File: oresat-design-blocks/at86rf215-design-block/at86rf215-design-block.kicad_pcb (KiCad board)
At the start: 4 copper layers, 69.4 x 52.5 mm, 61 parts, among them J1 SMA, J2 USB4105-GF-A, J4 SMA, J7 SMA, J8 SMA, J9 Screw_Terminal_01x02, SW1 RESET, U1 AT86RF215, U2 LP2985AIM5-1.8_NOPB, U3 2450FB15A050E, U5 QPC1022, U7 NCS2-62+, X1 TXETALSANF-26.000000

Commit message: more routing progress
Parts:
- moved C27 15.6 mm to (125.4, 78.7), turned to 0 degrees
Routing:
- net Net-(J7-In): track 0.00 -> 3.11 mm
- net Net-(J4-In): track 0.00 -> 3.01 mm
- net Net-(J8-In): track 0.00 -> 2.99 mm
- net Net-(C19-Pad1): track 0.00 -> 2.93 mm
- net Net-(C19-Pad2): track 0.00 -> 2.72 mm
- net Net-(C20-Pad2): track 0.00 -> 2.54 mm
- net Net-(C17-Pad1): track 1.66 -> 3.32 mm
- net Net-(C18-Pad2): track 1.66 -> 3.31 mm
- net Net-(U5-RF_COM): track 0.00 -> 1.59 mm
- net Net-(C20-Pad1): track 0.00 -> 1.59 mm
- net GND: vias 55 -> 58
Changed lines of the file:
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@@
 	(footprint "oresat-passives:0402-C"
 		(layer "F.Cu")
-		(at 140.97 79.545 -90)
+		(at 125.38 78.67)
 		(descr "<b>0402 (metric 1005) tight 'IPC-C'</b>\n<br>In house package for minimum spacing based on IPC-7351B.")
 		(property "Reference" "C27"
-			(at -0.7 -0.6 90)
+			(at -0.7 -0.6 0)
 			(layer "F.SilkS")
 			(effects
@@
 					(thickness 0.125)
 				)
-				(justify right top)
+				(justify left bottom)
 			)
 		)
 		(property "Value" "100p"
-			(at -0.7 1.4 90)
+			(at -0.7 1.4 0)
 			(layer "F.Fab")
 			(effects
@@
 					(thickness 0.12)
 				)
-				(justify right top)
+				(justify left bottom)
 			)
 		)
 		(property "Datasheet" "~"
-			(at 0 0 90)
+			(at 0 0 0)
 			(layer "F.Fab")
 			(hide yes)
@@
 		)
 		(property "Description" "CAP CER 100PF 50V C0G/NP0 0402"
-			(at 0 0 90)
+			(at 0 0 0)
 			(layer "F.Fab")
 			(hide yes)
@@
 		)
 		(property "DPN" "490-GCM1555C1H101GA16DCT-ND "
-			(at 0 0 270)
+			(at 0 0 0)
 			(unlocked yes)
 			(layer "F.Fab")
@@
 		)
 		(property "MFR" "Murata Electronics"
-			(at 0 0 270)
+			(at 0 0 0)
 			(unlocked yes)
 			(layer "F.Fab")
@@
 		)
 		(property "MPN" "GCM1555C1H101GA16D "
-			(at 0 0 270)
+			(at 0 0 0)
 			(unlocked yes)
 			(layer "F.Fab")
@@
 		)
 		(property "DIS" "DigiKey"
-			(at 0 0 270)
+			(at 0 0 0)
 			(unlocked yes)
 			(layer "F.Fab")
@@
 		)
 		(fp_line
+			(start -0.795 -0.395)
+			(end -0.795 0.395)
+			(stroke
+				(width 0.01)
+				(type solid)
+			)
+			(layer "F.CrtYd")
+		)
+		(fp_line
 			(start -0.795 0.395)
 			(end 0.795 0.395)
@@
 		)
 		(fp_line
+			(start 0.795 -0.395)
+			(end -0.795 -0.395)
+			(stroke
+				(width 0.01)
+				(type solid)
+			)
+			(layer "F.CrtYd")
+		)
+		(fp_line
 			(start 0.795 0.395)
 			(end 0.795 -0.395)
@@
 		)
 		(fp_line
-			(start -0.795 -0.395)
-			(end -0.795 0.395)
-			(stroke
-				(width 0.01)
-				(type solid)
-			)
-			(layer "F.CrtYd")
-		)
-		(fp_line
-			(start 0.795 -0.395)
-			(end -0.795 -0.395)
-			(stroke
-				(width 0.01)
-				(type solid)
-			)
-			(layer "F.CrtYd")
+			(start -0.525 -0.275)
+			(end 0.525 -0.275)
+			(stroke
+				(width 0.05)
+				(type solid)
+			)
+			(layer "F.Fab")
 		)
 		(fp_line
@@
 		)
 		(fp_line
+			(start 0.525 -0.275)
+			(end 0.525 0.275)
+			(stroke
+				(width 0.05)
+				(type solid)
+			)
+			(layer "F.Fab")
+		)
+		(fp_line
 			(start 0.525 0.275)
 			(end -0.525 0.275)
-			(stroke
-				(width 0.05)
-				(type solid)
-			)
-			(layer "F.Fab")
-		)
-		(fp_line
-			(start -0.525 -0.275)
-			(end 0.525 -0.275)
-			(stroke
-				(width 0.05)
-				(type solid)
-			)
-			(layer "F.Fab")
-		)
-		(fp_line
-			(start 0.525 -0.275)
-			(end 0.525 0.275)
 			(stroke
 				(width 0.05)
@@
 		)
 		(pad "1" smd roundrect
-			(at -0.45 0 270)
+			(at -0.45 0)
 			(size 0.5 0.6)
 			(layers "F.Cu" "F.Mask" "F.Paste")
@@
 		)
 		(pad "2" smd roundrect
-			(at 0.45 0 270)
+			(at 0.45 0)
 			(size 0.5 0.6)
 			(layers "F.Cu" "F.Mask" "F.Paste")
@@
 		(start 125.3286 82.1686)
 		(end 125.33 82.17)
-		(width 0.2)
+		(width 0.25)
 		(layer "F.Cu")
 		(net 20)
@@
 		(start 122.7525 82.1686)
 		(end 125.3286 82.1686)
-		(width 0.2)
+		(width 0.25)
 		(layer "F.Cu")
 		(net 20)
@@
 	)
 	(via
+		(at 140.22 84.91)
+		(size 0.4572)
+		(drill 0.254)
+		(layers "F.Cu" "B.Cu")
+		(free yes)
+		(net 25)
+	)
+	(via
 		(at 130.85 79.685001)
 		(size 0.4572)
@@
 	)
 	(via
+		(at 137.1 86.37)
+		(size 0.4572)
+		(drill 0.254)
+		(layers "F.Cu" "B.Cu")
+		(free yes)
+		(net 25)
+	)
+	(via
 		(at 123.335 86.6386)
+		(size 0.4572)
+		(drill 0.254)
+		(layers "F.Cu" "B.Cu")
+		(free yes)
+		(net 25)
+	)
+	(via
+		(at 141.74 84.9)
 		(size 0.4572)
 		(drill 0.254)
@@
 	)
 	(segment
+		(start 128.54 82.17)
+		(end 129.44 82.17)
+		(width 0.25)
+		(layer "F.Cu")
+		(net 38)
+	)
+	(segment
 		(start 126.88 82.17)
 		(end 128.53 82.17)
@@
 	)
 	(segment
+		(start 128.535 82.175)
+		(end 128.54 82.17)
+		(width 0.25)
+		(layer "F.Cu")
+		(net 38)
+	)
+	(segment
+		(start 129.44 82.17)
+		(end 129.6114 82.3414)
+		(width 0.25)
+		(layer "F.Cu")
+		(net 38)
+	)
+	(segment
 		(start 128.53 82.23)
 		(end 128.535 82.235)
@@
 	)
 	(segment
+		(start 129.6114 82.3414)
+		(end 130.120001 82.3414)
+		(width 0.25)
+		(layer "F.Cu")
+		(net 38)
+	)
+	(segment
 		(start 128.535 83.75)
 		(end 126.88 83.75)
@@
 		(layer "F.Cu")
 		(net 39)
+	)
+	(segment
+		(start 128.535 83.75)
+		(end 129.48 83.75)
+		(width 0.25)
+		(layer "F.Cu")
+		(net 39)
+	)
+	(segment
+		(start 129.48 83.75)
+		(end 129.6386 83.5914)
+		(width 0.25)
+		(layer "F.Cu")
+		(net 39)
+	)
+	(segment
+		(start 129.6386 83.5914)
+		(end 130.120001 83.5914)
+		(width 0.25)
+		(layer "F.Cu")
+		(net 39)
+	)
+	(segment
+		(start 132.75 82.3414)
+		(end 134.135 82.3414)
+		(width 0.127)
+		(layer "F.Cu")
+		(net 40)
+	)
+	(segment
+		(start 131.419999 82.3414)
+		(end 132.75 82.3414)
+		(width 0.127)
+		(layer "F.Cu")
+		(net 40)
+	)
+	(segment
+		(start 137.1 82.3414)
+		(end 137.1 83.8564)
+		(width 0.127)
+		(layer "F.Cu")
+		(net 41)
+	)
+	(segment
+		(start 135.685 82.3414)
+		(end 137.1 82.3414)
+		(width 0.127)
+		(layer "F.Cu")
+		(net 41)
+	)
+	(segment
+		(start 138.75 82.3414)
+		(end 140.2186 82.3414)
+		(width 0.127)
+		(layer "F.Cu")
+		(net 42)
+	)
+	(segment
+		(start 140.2186 82.3414)
+		(end 140.22 82.34)
+		(width 0.127)
+		(layer "F.Cu")
+		(net 42)
+	)
+	(segment
+		(start 140.22 82.34)
+		(end 141.755 82.34)
+		(width 0.127)
+		(layer "F.Cu")
+		(net 42)
+	)
+	(segment
+		(start 141.755 82.34)
+		(end 141.76 82.345)
+		(width 0.127)
+		(layer "F.Cu")
+		(net 42)
 	)
 	(segment
@@
 		(net 50)
 	)
+	(segment
+		(start 132.155799 78.68)
+		(end 132.1608 78.685001)
+		(width 0.127)
+		(layer "F.Cu")
+		(net 53)
+	)
+	(segment
+		(start 129.619999 78.68)
+		(end 132.155799 78.68)
+		(width 0.127)
+		(layer "F.Cu")
+		(net 53)
+	)
+	(segment
+		(start 133.7108 78.685001)
+		(end 133.7108 77.1008)
+		(width 0.127)
+		(layer "F.Cu")
+		(net 54)
+	)
+	(segment
+		(start 133.7108 77.1008)
+		(end 133.71 77.1)
+		(width 0.127)
+		(layer "F.Cu")
+		(net 54)
+	)
+	(segment
+		(start 135.1892 78.683401)
+		(end 135.1908 78.685001)
+		(width 0.127)
+		(layer "F.Cu")
+		(net 55)
+	)
+	(segment
+		(start 135.1892 77.1)
+		(end 135.1892 78.683401)
+		(width 0.127)
+		(layer "F.Cu")
+		(net 55)
+	)
+	(segment
+		(start 149.07 79.99)
+		(end 152.1775 79.99)
+		(width 0.127)
+		(layer "F.Cu")
+		(net 57)
+	)
+	(segment
+		(start 149.18 71.62)
+		(end 152.16625 71.62)
+		(width 0.127)
+		(layer "F.Cu")
+		(net 58)
+	)
+	(segment
+		(start 152.16625 71.62)
+		(end 152.1675 71.62125)
+		(width 0.127)
+		(layer "F.Cu")
+		(net 58)
+	)
 	(zone

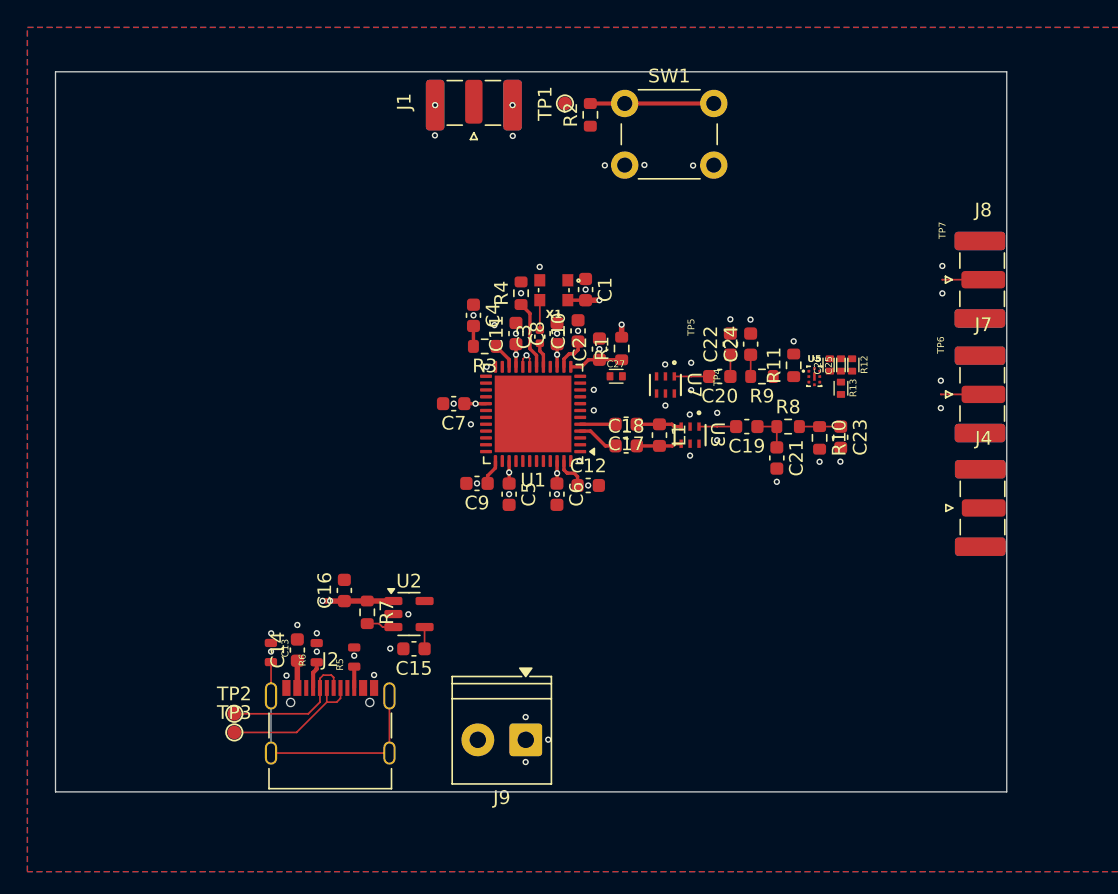
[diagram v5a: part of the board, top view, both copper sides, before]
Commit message: completed initial routing, changed pin out and added voltage divider to QPC1022 CTRL pin
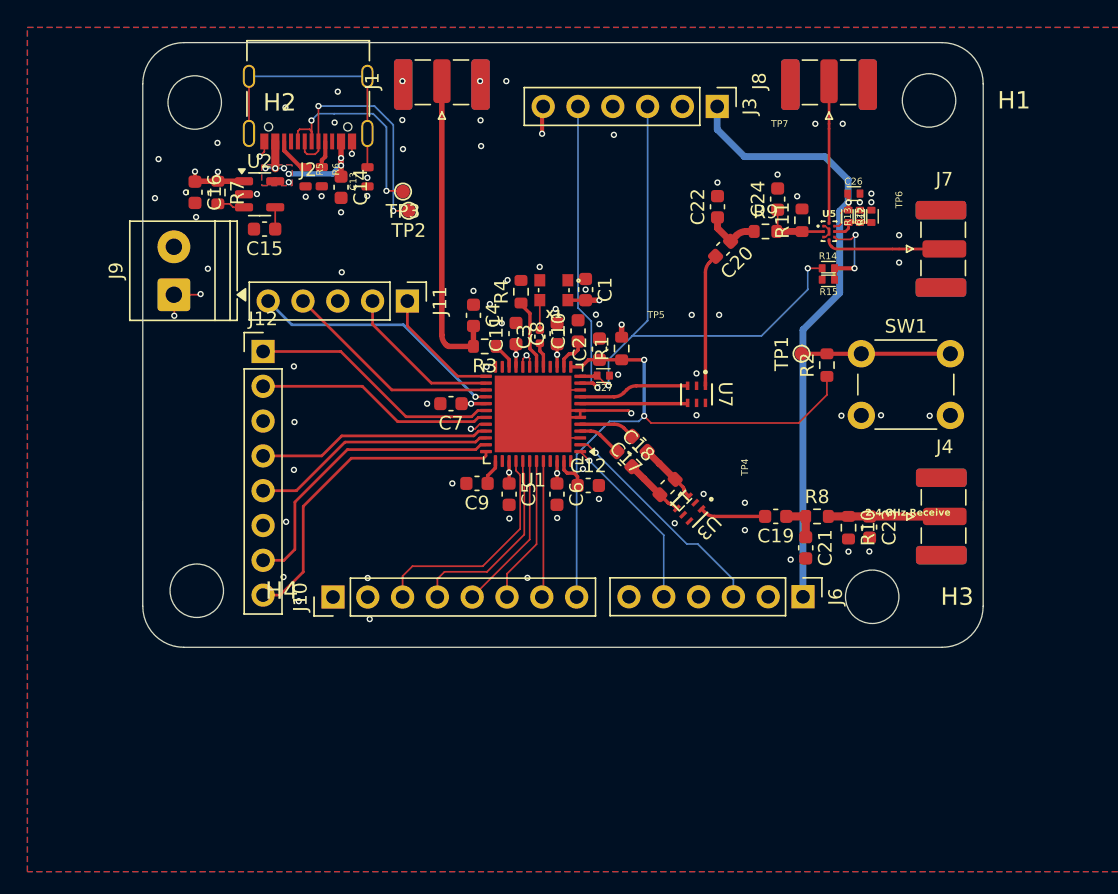
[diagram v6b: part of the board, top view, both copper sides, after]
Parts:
- added H1: MountingHole, oresat-misc:M2-Press-Fit-Nut, F.Cu at (148.2, 58.5)
- added H2: MountingHole, oresat-misc:M2-Press-Fit-Nut, F.Cu at (94.6, 58.7)
- added H3: MountingHole, oresat-misc:M2-Press-Fit-Nut, F.Cu at (144.1, 94.8)
- added H4: MountingHole, oresat-misc:M2-Press-Fit-Nut, F.Cu at (94.8, 94.3)
- added J10: Conn_01x08, Connector_PinHeader_2.54mm:PinHeader_1x08_P2.54mm_Vertical, F.Cu at (104.7, 94.8)
- added J11: Conn_01x05, Connector_PinHeader_2.54mm:PinHeader_1x05_P2.54mm_Vertical, F.Cu at (110.1, 73.2)
- added J12: Conn_01x08, Connector_PinHeader_2.54mm:PinHeader_1x08_P2.54mm_Vertical, F.Cu at (99.6, 76.9)
- added J3: Conn_01x06, Connector_PinHeader_2.54mm:PinHeader_1x06_P2.54mm_Vertical, F.Cu at (132.8, 59.0)
- added J6: Conn_01x06, Connector_PinHeader_2.54mm:PinHeader_1x06_P2.54mm_Vertical, F.Cu at (139.0, 94.8)
- added R14: 3k, oresat-passives:0402-C, F.Cu at (140.9, 70.8)
- added R15: 5k, oresat-passives:0402-C, F.Cu at (140.9, 71.6)
- moved J2 44.9 mm to (102.9, 59.0), turned to 180 degrees
- moved J9 41.4 mm to (93.1, 72.7), turned to 90 degrees
- moved TP3 41.3 mm to (109.8, 65.2), turned to 180 degrees
- moved TP2 38.9 mm to (110.2, 66.6), turned to 180 degrees
- moved C13 35.4 mm to (107.2, 64.1), turned to 90 degrees
- moved R5 35.2 mm to (102.7, 64.1), turned to -90 degrees
- moved R6 34.7 mm to (103.9, 64.1), turned to -90 degrees
- moved C14 33.9 mm to (105.3, 64.9), turned to -90 degrees
- moved C15 32.5 mm to (99.7, 67.9)
- moved R7 32.5 mm to (96.3, 65.3)
- moved U2 32.5 mm to (99.4, 65.4)
- moved C16 31.0 mm to (94.6, 65.2), turned to -90 degrees
- moved TP1 25.1 mm to (138.9, 77.0)
- moved R2 25.1 mm to (140.8, 77.9)
- moved SW1 25.1 mm to (143.3, 77.0)
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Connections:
- C27 pad 1: FEA09 -> GND
- C27 pad 2: GND -> FEA09
- U5 pad 5: FEA09 -> Net-(U5-CTRL)
- U7 pad 3: RFN09 -> RFP09
- U7 pad 4: RFP09 -> RFN09
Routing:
- net +5V: track 1.99 -> 105.9 mm, vias 0 -> 8
- net FEA09: track 0.00 -> 40.7 mm, vias 0 -> 2
- net ~{RSTN}: track 3.93 -> 41.9 mm, vias 0 -> 2
- net GND: track 1.89 -> 31.8 mm, vias 58 -> 82
- net RXDP24: track 0.00 -> 23.6 mm
- net FEB09: track 0.00 -> 22.5 mm, vias 0 -> 1
- net RXDN24: track 0.00 -> 21.8 mm
- net CLKO: track 1.49 -> 22.9 mm
- net TXDP: track 0.00 -> 18.8 mm, vias 0 -> 1
- net RXDN09: track 0.00 -> 18.4 mm
- net RXCLKP: track 0.00 -> 17.9 mm
- net RXDP09: track 0.00 -> 17.5 mm
- net RXCLKN: track 0.00 -> 17.0 mm
- net INTERRUPT: track 0.00 -> 16.6 mm
- net FEA24: track 0.00 -> 16.5 mm, vias 0 -> 1
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- added copper zone on B.Cu, net +5V
- added copper zone on F.Cu, net +5V
- added copper zone on In2.Cu, net +5V
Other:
- board size 69.4 x 52.5 mm -> 61.3 x 44.1 mm
- board text added: "2.4 GHz Receive"

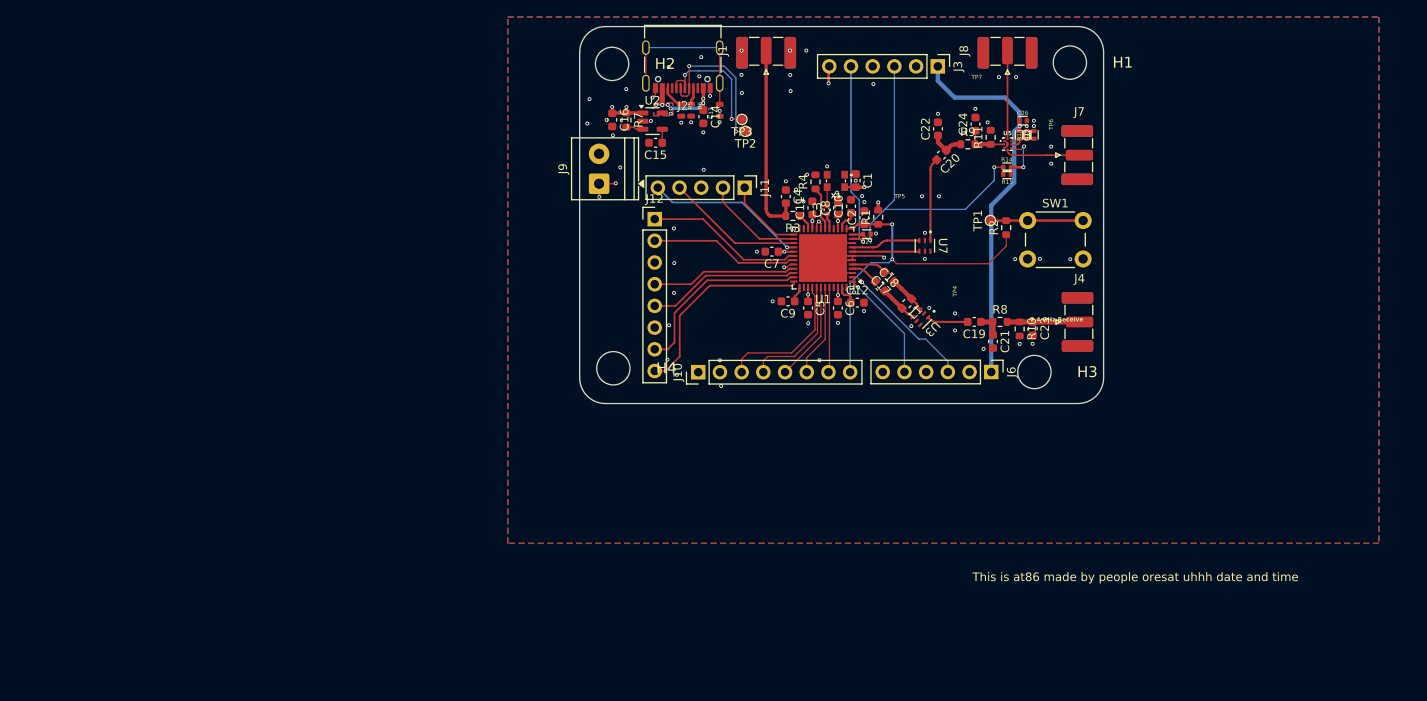
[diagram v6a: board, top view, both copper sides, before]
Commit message: Finish routing and silk screen layout, added ground stitching on border and RF lines
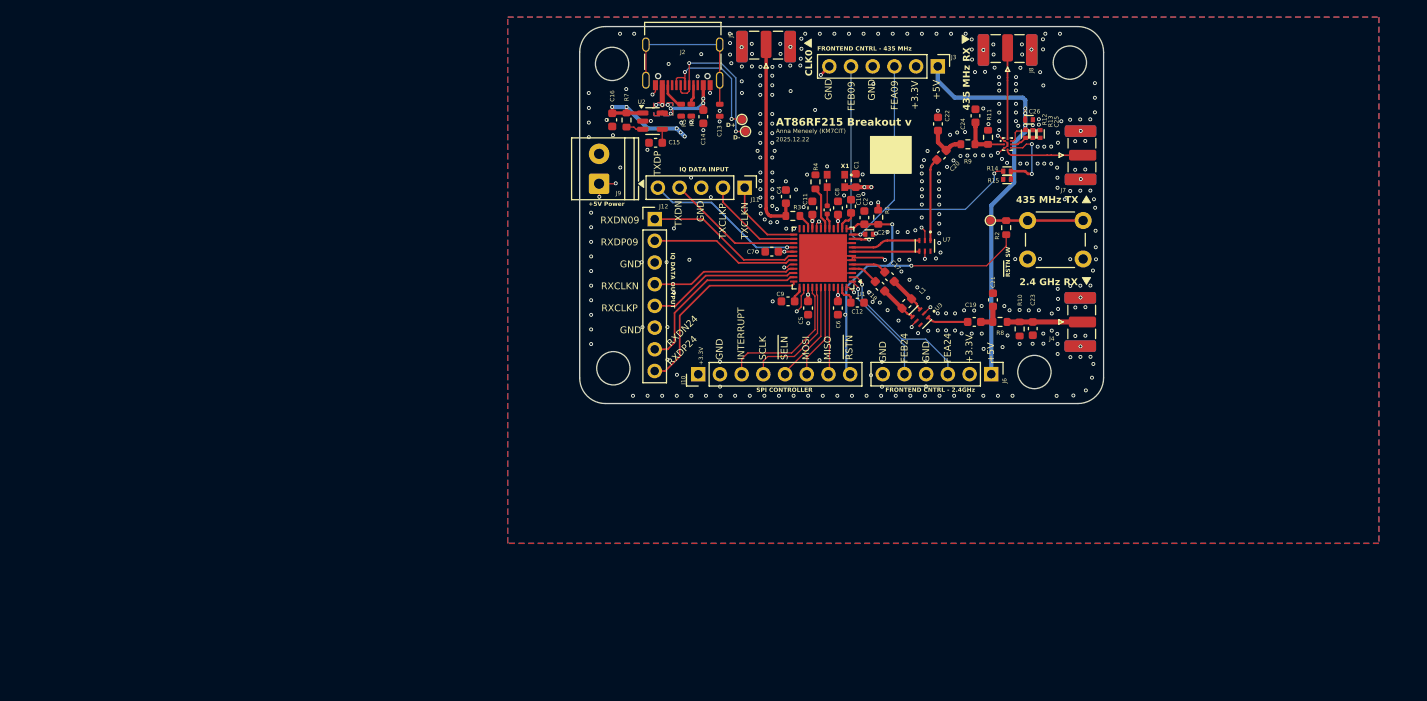
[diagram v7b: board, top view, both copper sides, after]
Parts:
- added G***: LOGO, LOGO, B.Cu at (124.9, 82.1)
- added TP10: ~, oresat-misc:TestPoint_RF_Probe, F.Cu at (112.7, 68.9)
- added TP8: ~, oresat-misc:TestPoint_RF_Probe, F.Cu at (146.1, 88.9)
- added TP9: ~, oresat-misc:TestPoint_RF_Probe, F.Cu at (139.8, 68.1)
- moved C21 4.87 mm to (139.2, 86.3), turned to 90 degrees
- moved C24 0.97 mm to (137.2, 64.8)
- moved J1 0.72 mm to (112.7, 56.4)
- moved C25 0.72 mm to (144.7, 66.9)
- moved C26 0.72 mm to (143.4, 65.2)
- moved R13 0.72 mm to (143.9, 66.9)
- moved R12 0.72 mm to (143.0, 66.9)
- moved R15 0.59 mm to (140.9, 72.2)
- moved C22 0.58 mm to (132.8, 65.7)
- moved R14 0.46 mm to (140.9, 71.2)
- moved J7 0.38 mm to (149.7, 69.4)
- moved J2 0.35 mm to (102.9, 58.7)
- moved J4 0.33 mm to (149.7, 88.9)
- moved J8 0.33 mm to (140.9, 56.8)
- moved R11 0.31 mm to (138.6, 67.3)
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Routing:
- net +3.3V: track 16.3 -> 129.8 mm, vias 9 -> 13
- net GND: track 31.8 -> 42.2 mm, vias 82 -> 354
- net +5V: track 105.9 -> 110.7 mm, vias 8 -> 10
- net Net-(U5-CTRL): track 6.51 -> 9.66 mm
- net FEB09: track 22.5 -> 24.0 mm
- net FEA24: track 16.5 -> 17.9 mm
- net ~{RSTN}: track 41.9 -> 43.1 mm
- net FEA09: track 40.7 -> 39.6 mm
- net Net-(U5-RF_COM): track 5.00 -> 5.97 mm
- net CLKO: track 22.9 -> 23.6 mm
- net TXCLKN: track 9.08 -> 9.67 mm
- net Net-(C20-Pad1): track 4.12 -> 4.70 mm
- net Net-(U5-EN): track 3.22 -> 3.72 mm
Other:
- board text added: "${ISSUE_DATE}"
- board text added: "+3.3V"
- board text added: "+5V"
- board text added: "+5V Power"
- board text added: "2.4 GHz RX"
- board text added: "2025.12.22"
- board text added: "435 MHz RX"
- board text added: "435 MHz TX"
- board text added: "AT86RF215 Breakout v${REVISION}"
- board text added: "Angry Cat declares this board WILL work! Or ELSE!"
- board text added: "Anna Meneely (KM7CIT)"
- board text added: "CLK0"
- board text added: "D+"
- board text added: "D-"
- board text added: "FEA09"
- board text added: "FEA24"
- board text added: "FEB09"
- board text added: "FEB24"
- board text added: "FRONTEND CNTRL - 2.4GHz"
- board text added: "FRONTEND CNTRL - 435 MHz"
- board text added: "GND"
- board text added: "INTERRUPT"
- board text added: "IQ DATA INPUT"
- board text added: "IQ DATA OUTPUT"
- board text added: "MISO"
- board text added: "MOSI"
- board text added: "RSTN"
- board text added: "RSTN SW"
- board text added: "RXCLKN"
- board text added: "RXCLKP"
- board text added: "RXDN09"
- board text added: "RXDN24"
- board text added: "RXDP09"
- board text added: "RXDP24"
- board text added: "SCLK"
- board text added: "SELN"
- board text added: "SPI CONTROLLER"
- board text added: "TXCLKN"
- board text added: "TXCLKP"
- board text added: "TXDN"
- board text added: "TXDP"
- board text removed: "2.4 GHz Receive"
- board text removed: "This is at86 made by people oresat uhhh date and time"
